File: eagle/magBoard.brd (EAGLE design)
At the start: 100 x 80 mm, 9 parts, among them J1 RJ11-6PTH, U3 MAX232PTH

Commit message: updated magBoard and thesis files, added a couple boards and schematics for references or parts.
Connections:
- net N$1 renamed RX
- net N$13 renamed GND
- net N$6 renamed TX
- net N$7 renamed VH
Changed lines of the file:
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@@
 <wire x1="72.136" y1="41.656" x2="72.136" y2="38.1" width="0.254" layer="1"/>
 </signal>
-<signal name="N$7">
+<signal name="VH">
 <contactref element="U3" pad="16"/>
 <contactref element="C4" pad="1"/>
@@
 <wire x1="59.309" y1="34.925" x2="66.929" y2="34.925" width="0.254" layer="16"/>
 </signal>
-<signal name="N$13">
+<signal name="GND">
 <contactref element="U3" pad="15"/>
 <contactref element="MAG" pad="5"/>
@@
 <wire x1="88.138" y1="46.101" x2="88.242" y2="46.204" width="0.254" layer="1"/>
 </signal>
-<signal name="N$1">
+<signal name="RX">
 <contactref element="U3" pad="12"/>
 <contactref element="J1" pad="3"/>
@@
 <wire x1="74.803" y1="52.451" x2="73.533" y2="51.181" width="0.254" layer="1"/>
 </signal>
-<signal name="N$6">
+<signal name="TX">
 <contactref element="J1" pad="4"/>
 <contactref element="U3" pad="11"/>

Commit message: changes to eagle files
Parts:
- moved C4 61.2 mm to (25.4, 18.3)
- moved MAG 61.2 mm to (33.1, 20.1)
- moved R1 61.2 mm to (25.0, 25.8)
- moved C2 61.2 mm to (24.6, 31.4)
- moved C3 61.2 mm to (2.79, 17.4)
- moved C5 61.2 mm to (17.0, 18.3)
- moved C6 61.2 mm to (2.79, 10.2)
- moved J1 61.2 mm to (9.40, 33.5)
- moved U3 61.2 mm to (17.1, 10.7)
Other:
- board size 100 x 80 mm -> 41.6 x 40.5 mm

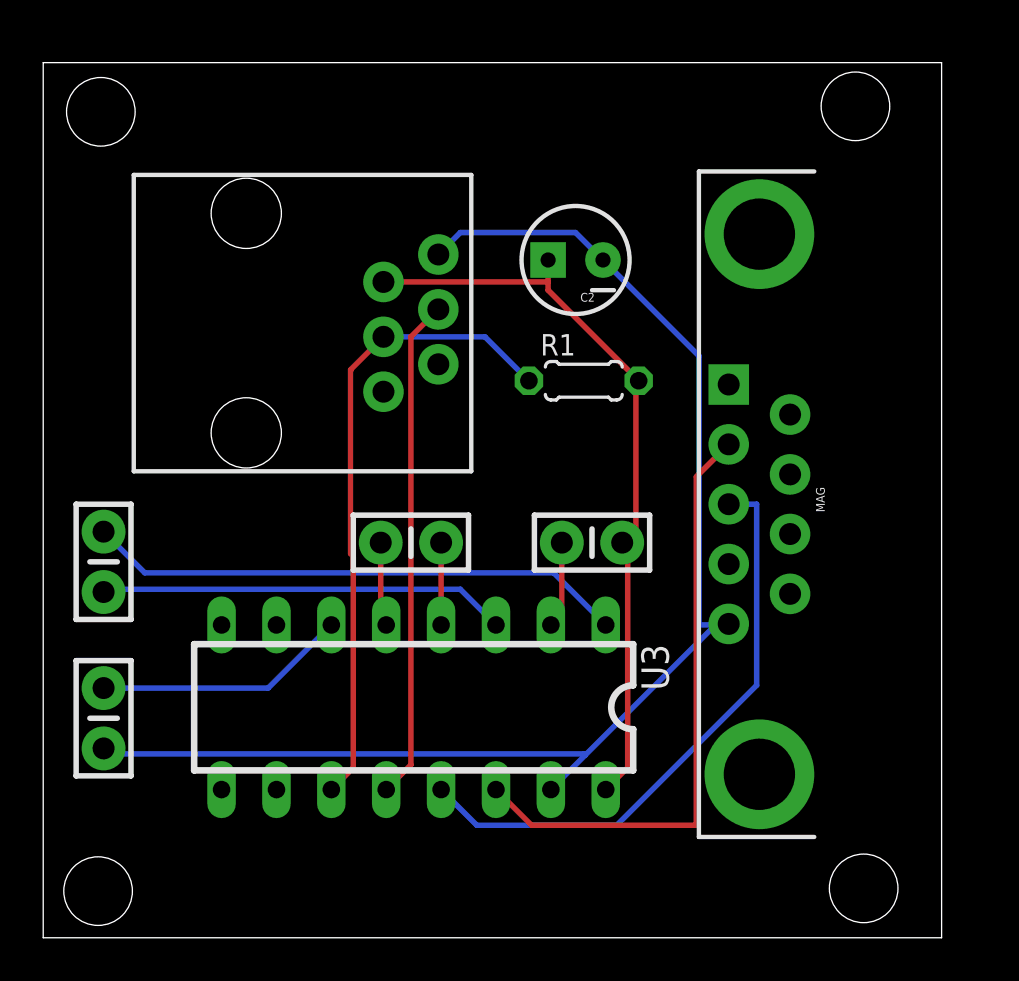
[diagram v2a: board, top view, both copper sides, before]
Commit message: eagle file changes that were submitted for a quote
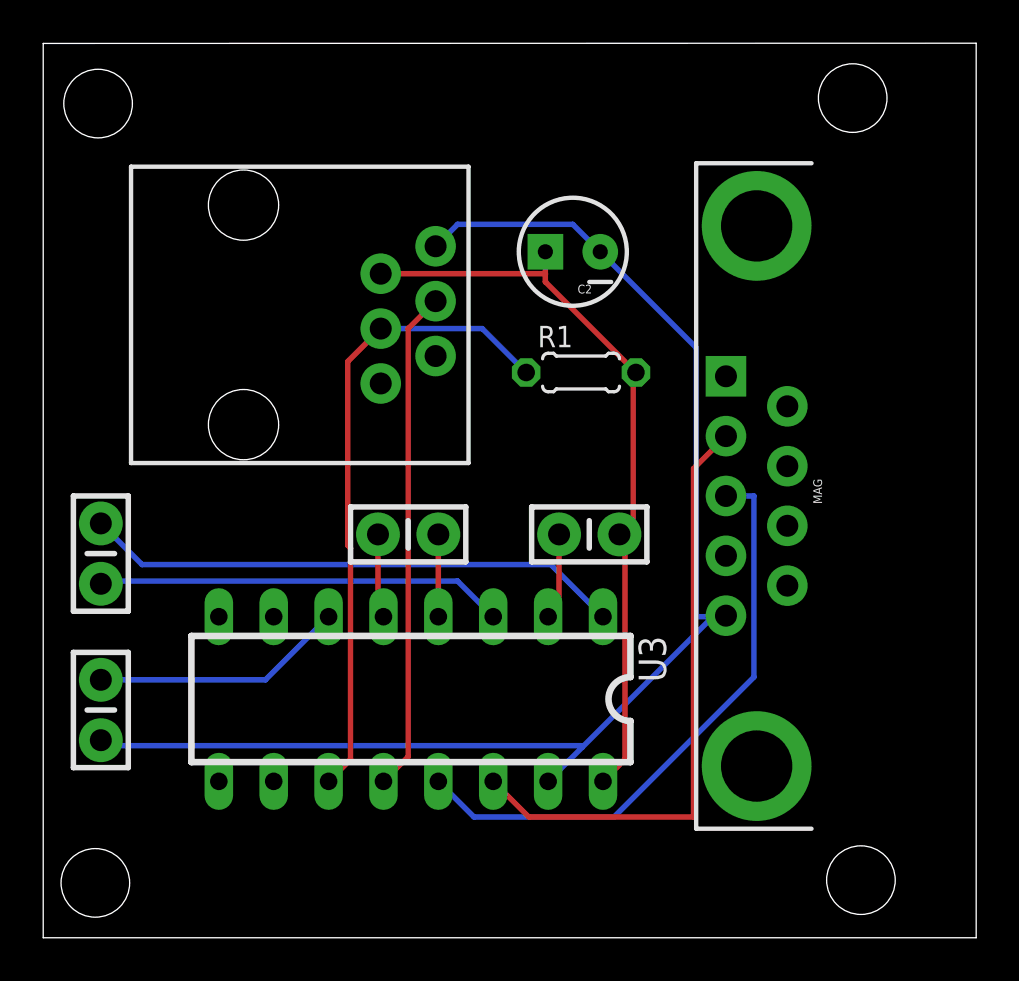
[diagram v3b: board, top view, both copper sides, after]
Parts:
- moved C2 0.40 mm to (24.5, 31.8)
- moved C5 0.40 mm to (16.9, 18.7)
- moved C3 0.40 mm to (2.67, 17.8)
- moved C6 0.40 mm to (2.67, 10.5)
- moved C4 0.40 mm to (25.3, 18.7)
- moved J1 0.40 mm to (9.27, 33.9)
- moved R1 0.40 mm to (24.9, 26.2)
- moved U3 0.40 mm to (17.0, 11.0)
- moved MAG 0.40 mm to (33.0, 20.4)
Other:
- board size 41.6 x 40.5 mm -> 43.2 x 41.4 mm
- board text added: "ADAM CHASE 07/29/13 TTL-RS232 v1.00"

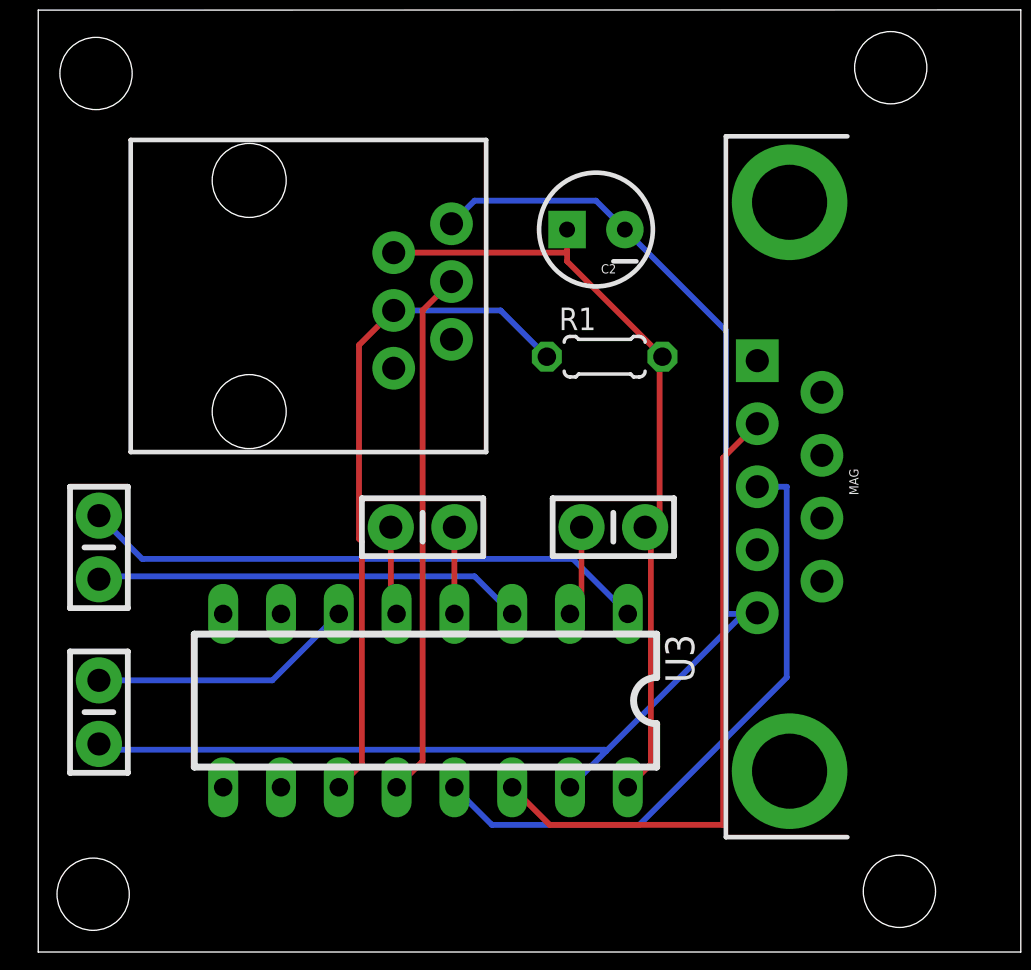
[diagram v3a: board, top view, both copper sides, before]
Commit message: made board revision to v2.0 and ready to order, pending BOM
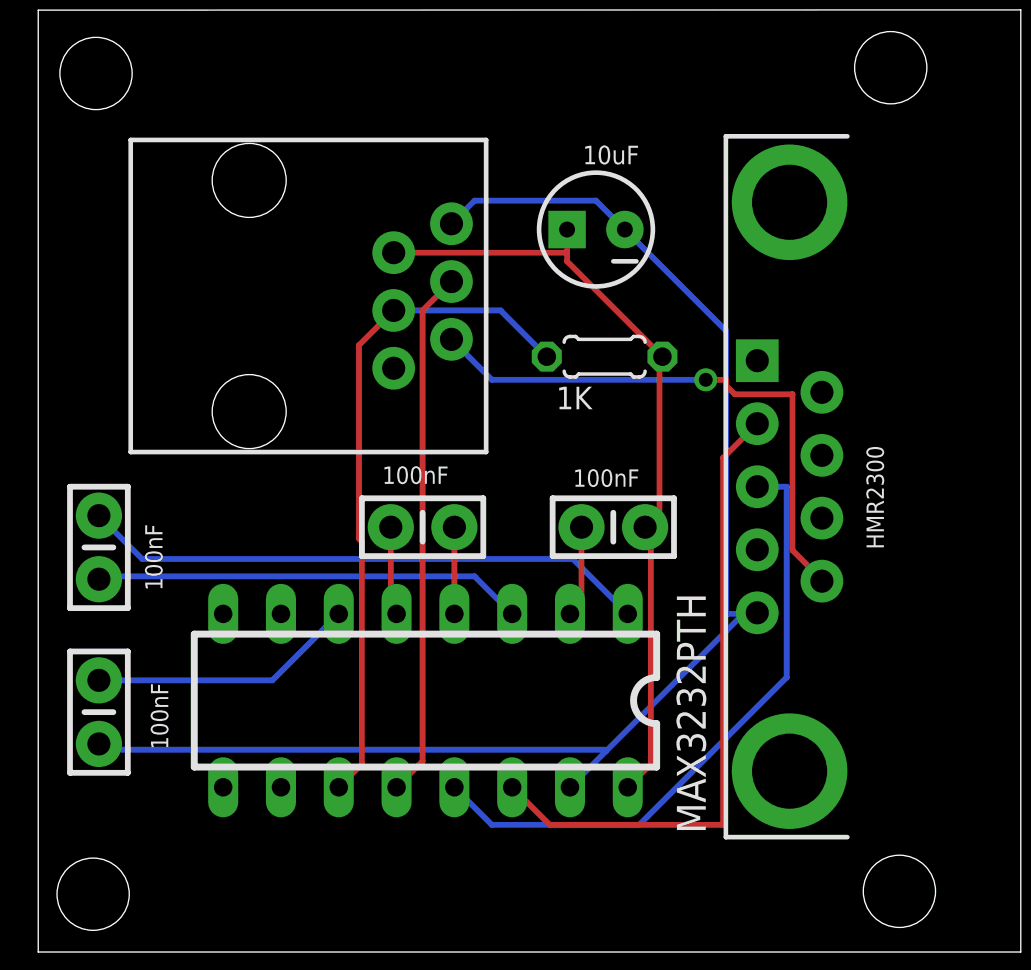
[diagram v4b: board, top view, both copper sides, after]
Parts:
- U3: value MAX232PTH -> MAX3232PTH
- renumbered MAG to HMR2300
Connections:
- net N$16 renamed RS232IN
- net N$17 renamed RS232DO
- net RX renamed DO
- net TX renamed DI
- net VH renamed 33V
- new net VIN: HMR2300.9, J1.5
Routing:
- net VIN: track 0.00 -> 24.9 mm, vias 0 -> 1
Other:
- board text added: "100nF"
- board text added: "ADAM CHASE 08/13/13"
- board text added: "TTL-RS232 v1.10"
- board text removed: "ADAM CHASE 07/29/13 TTL-RS232 v1.00"
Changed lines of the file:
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@@
 <hole x="37.846" y="2.667" drill="3.175"/>
 <hole x="37.465" y="38.862" drill="3.175"/>
-<text x="6.223" y="29.591" size="1.778" layer="22" rot="MR270" align="center">ADAM CHASE
-07/29/13
-TTL-RS232
-v1.00
+<text x="21.082" y="37.338" size="1.778" layer="22" rot="MR0" align="center">ADAM CHASE
+08/13/13
 </text>
+<text x="21.082" y="2.413" size="1.778" layer="22" rot="MR0" align="center">TTL-RS232
+v1.10</text>
+<text x="15.113" y="20.574" size="0.762" layer="21">100nF</text>
+<text x="23.495" y="20.447" size="0.762" layer="21">100nF</text>
+<text x="5.461" y="15.875" size="0.762" layer="21" rot="R90">100nF</text>
+<text x="5.715" y="8.89" size="0.762" layer="21" rot="R90">100nF</text>
 </plain>
 <attributes>
@@
 </autorouter>
 <elements>
-<element name="U3" library="SparkFun-DigitalIC" package="DIL16" value="MAX232PTH" x="17.018" y="11.049" rot="R180"/>
+<element name="U3" library="SparkFun-DigitalIC" package="DIL16" value="MAX3232PTH" x="17.018" y="11.049" smashed="yes" rot="R180">
+<attribute name="VALUE" x="29.337" y="5.207" size="1.27" layer="25" ratio="10" rot="R90"/>
+</element>
 <element name="C4" library="SparkFun-Capacitors" package="CAP-PTH-SMALL-KIT" value="100nF" x="25.273" y="18.669" rot="R180"/>
 <element name="C3" library="SparkFun-Capacitors" package="CAP-PTH-SMALL-KIT" value="100nF" x="2.667" y="17.78" rot="R270"/>
 <element name="C5" library="SparkFun-Capacitors" package="CAP-PTH-SMALL-KIT" value="100nF" x="16.891" y="18.669" rot="R180"/>
 <element name="C6" library="SparkFun-Capacitors" package="CAP-PTH-SMALL-KIT" value="100nF" x="2.667" y="10.541" rot="R270"/>
-<element name="MAG" library="SparkFun-Connectors" package="DB9" value="RS232" x="33.02" y="20.447" rot="R270"/>
+<element name="HMR2300" library="SparkFun-Connectors" package="DB9" value="RS232" x="33.02" y="20.447" smashed="yes" rot="R270">
+<attribute name="NAME" x="36.402" y="22.258" size="0.762" layer="21" ratio="10" rot="R270"/>
+<attribute name="VALUE" x="38.213" y="21.264" size="0.762" layer="27" ratio="10" rot="R270"/>
+</element>
 <element name="J1" library="SparkFun-Connectors" package="RJ11-6" value="RJ11-6PTH" x="9.271" y="33.909" rot="R270"/>
-<element name="R1" library="rcl" package="0204/5" value="1K" x="24.892" y="26.162"/>
-<element name="C2" library="SparkFun-Capacitors" package="CPOL-RADIAL-10UF-25V" value="10uF" x="24.511" y="31.75" rot="R180"/>
+<element name="R1" library="rcl" package="0204/5" value="1K" x="24.892" y="26.162" smashed="yes">
+<attribute name="VALUE" x="22.7584" y="23.8506" size="0.9906" layer="21" ratio="10"/>
+</element>
+<element name="C2" library="SparkFun-Capacitors" package="CPOL-RADIAL-10UF-25V" value="10uF" x="24.511" y="31.75" smashed="yes" rot="R180">
+<attribute name="VALUE" x="26.416" y="35.433" size="0.8128" layer="21" rot="R180"/>
+</element>
 </elements>
 <signals>
@@
 <wire x1="15.494" y1="18.669" x2="15.494" y2="15.113" width="0.254" layer="1"/>
 </signal>
-<signal name="VH">
+<signal name="33V">
 <contactref element="U3" pad="16"/>
 <contactref element="C4" pad="1"/>
@@
 <signal name="GND">
 <contactref element="U3" pad="15"/>
-<contactref element="MAG" pad="5"/>
+<contactref element="HMR2300" pad="5"/>
 <contactref element="J1" pad="1"/>
 <contactref element="C2" pad="2"/>
@@
 <wire x1="30.861" y1="14.859" x2="31.6" y2="14.907" width="0.254" layer="16"/>
 </signal>
-<signal name="N$16">
-<contactref element="MAG" pad="3"/>
+<signal name="RS232IN">
+<contactref element="HMR2300" pad="3"/>
 <contactref element="U3" pad="13"/>
 <wire x1="19.939" y1="5.588" x2="18.288" y2="7.239" width="0.254" layer="16"/>
@@
 <wire x1="31.6" y1="20.447" x2="32.893" y2="20.447" width="0.254" layer="16"/>
 </signal>
-<signal name="N$17">
-<contactref element="MAG" pad="2"/>
+<signal name="RS232DO">
+<contactref element="HMR2300" pad="2"/>
 <contactref element="U3" pad="14"/>
 <wire x1="22.479" y1="5.588" x2="20.828" y2="7.239" width="0.254" layer="1"/>
@@
 <wire x1="31.496" y1="23.114" x2="31.6" y2="23.217" width="0.254" layer="1"/>
 </signal>
-<signal name="RX">
+<signal name="DO">
 <contactref element="U3" pad="12"/>
 <contactref element="J1" pad="3"/>
@@
 <wire x1="18.161" y1="29.464" x2="16.891" y2="28.194" width="0.254" layer="1"/>
 </signal>
-<signal name="TX">
+<signal name="DI">
 <contactref element="J1" pad="4"/>
 <contactref element="U3" pad="11"/>
@@
 <wire x1="15.621" y1="28.194" x2="20.32" y2="28.194" width="0.254" layer="16"/>
 </signal>
+<signal name="VIN">
+<contactref element="HMR2300" pad="9"/>
+<contactref element="J1" pad="5"/>
+<wire x1="19.939" y1="25.146" x2="18.161" y2="26.924" width="0.254" layer="16"/>
+<wire x1="29.337" y1="25.146" x2="19.939" y2="25.146" width="0.254" layer="16"/>
+<wire x1="30.226" y1="25.146" x2="29.337" y2="25.146" width="0.254" layer="1"/>
+<wire x1="30.226" y1="24.892" x2="30.226" y2="25.146" width="0.254" layer="1"/>
+<wire x1="30.607" y1="24.511" x2="30.226" y2="24.892" width="0.254" layer="1"/>
+<wire x1="33.147" y1="24.511" x2="30.607" y2="24.511" width="0.254" layer="1"/>
+<wire x1="33.147" y1="17.653" x2="33.147" y2="24.511" width="0.254" layer="1"/>
+<wire x1="34.417" y1="16.383" x2="33.147" y2="17.653" width="0.254" layer="1"/>
+<wire x1="34.417" y1="16.383" x2="34.44" y2="16.297" width="0.254" layer="1"/>
+<via x="29.337" y="25.146" extent="1-16" drill="0.6096"/>
+</signal>
 </signals>
